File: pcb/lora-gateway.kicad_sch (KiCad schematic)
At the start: 2 parts, among them U1 RFM95W-868S2, U2 ATmega2560-16A

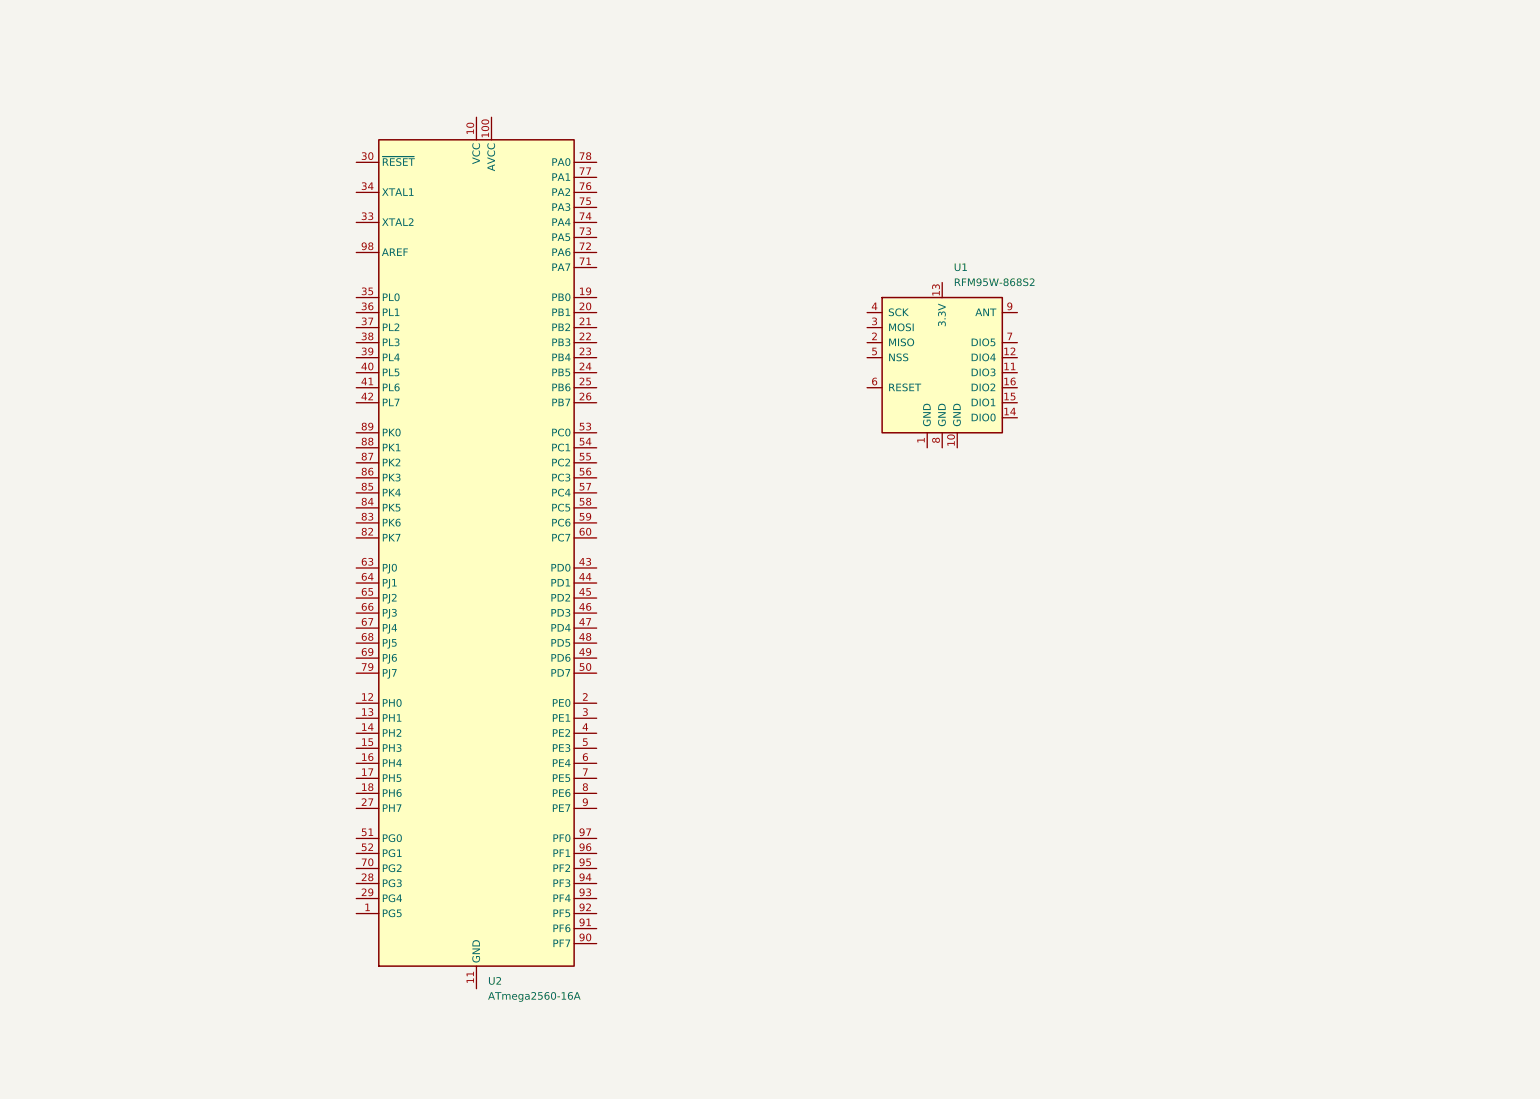
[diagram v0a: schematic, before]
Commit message: add m2560 + rfm95
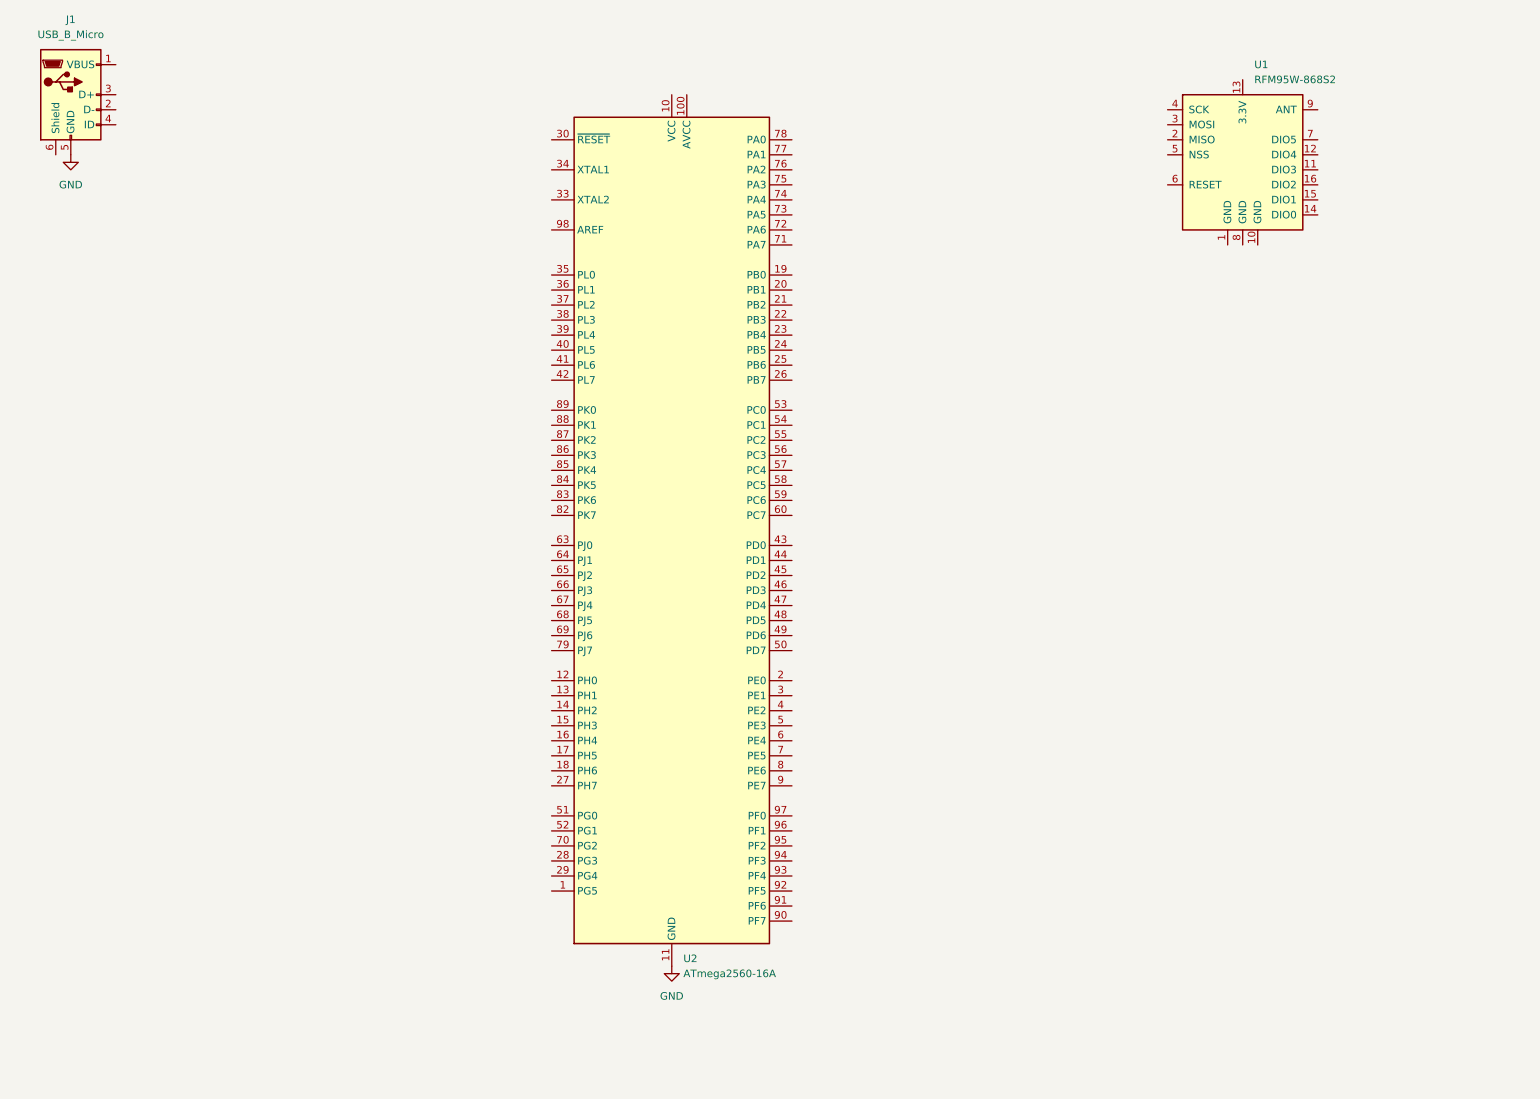
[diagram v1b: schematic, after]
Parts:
- added J1: USB_B_Micro, symbol Connector:USB_B_Micro
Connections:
- net GND: now reaches U2.11 (GND), U2.32 (GND), U2.62 (GND), U2.81 (GND), U2.99 (GND)
- net GND: now also J1.5 (GND)
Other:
- moved on the sheet: U1, U2
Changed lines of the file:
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@@
 (kicad_sch (version 20230121) (generator eeschema)
   (paper "A4")
-  (symbol (lib_id "MCU_Microchip_ATmega:ATmega2560-16A") (at 91.44 102.87 0) (unit 1)
-    (in_bom yes) (on_board yes) (dnp no) (fields_autoplaced)
-    (property "Reference" "U2" (at 93.3959 175.26 0)
-      (effects (font (size 1.27 1.27)) (justify left))
-    )
-    (property "Value" "ATmega2560-16A" (at 93.3959 177.8 0)
-      (effects (font (size 1.27 1.27)) (justify left))
-    )
-    (property "Footprint" "Package_QFP:TQFP-100_14x14mm_P0.5mm" (at 91.44 102.87 0)
+  (symbol (lib_id "MCU_Microchip_ATmega:ATmega2560-16A") (at 124.46 99.06 0) (unit 1)
+    (in_bom yes) (on_board yes) (dnp no) (fields_autoplaced)
+    (property "Reference" "U2" (at 126.4159 171.45 0)
+      (effects (font (size 1.27 1.27)) (justify left))
+    )
+    (property "Value" "ATmega2560-16A" (at 126.4159 173.99 0)
+      (effects (font (size 1.27 1.27)) (justify left))
+    )
+    (property "Footprint" "Package_QFP:TQFP-100_14x14mm_P0.5mm" (at 124.46 99.06 0)
       (effects (font (size 1.27 1.27) italic) hide)
     )
-    (property "Datasheet" "http://ww1.microchip.com/downloads/en/DeviceDoc/Atmel-2549-8-bit-AVR-Microcontroller-ATmega640-1280-1281-2560-2561_datasheet.pdf" (at 91.44 102.87 0)
+    (property "Datasheet" "http://ww1.microchip.com/downloads/en/DeviceDoc/Atmel-2549-8-bit-AVR-Microcontroller-ATmega640-1280-1281-2560-2561_datasheet.pdf" (at 124.46 99.06 0)
       (effects (font (size 1.27 1.27)) hide)
     )
@@
     )
   )
-  (symbol (lib_id "RF_Module:RFM95W-868S2") (at 170.18 69.85 0) (unit 1)
-    (in_bom yes) (on_board yes) (dnp no) (fields_autoplaced)
-    (property "Reference" "U1" (at 172.1359 54.61 0)
-      (effects (font (size 1.27 1.27)) (justify left))
-    )
-    (property "Value" "RFM95W-868S2" (at 172.1359 57.15 0)
-      (effects (font (size 1.27 1.27)) (justify left))
-    )
-    (property "Footprint" "" (at 86.36 27.94 0)
-      (effects (font (size 1.27 1.27)) hide)
-    )
-    (property "Datasheet" "https://www.hoperf.com/data/upload/portal/20181127/5bfcbea20e9ef.pdf" (at 86.36 27.94 0)
+  (symbol (lib_id "Connector:USB_B_Micro") (at 22.86 25.4 0) (unit 1)
+    (in_bom yes) (on_board yes) (dnp no) (fields_autoplaced)
+    (property "Reference" "J1" (at 22.86 12.7 0)
+      (effects (font (size 1.27 1.27)))
+    )
+    (property "Value" "USB_B_Micro" (at 22.86 15.24 0)
+      (effects (font (size 1.27 1.27)))
+    )
+    (property "Footprint" "" (at 26.67 26.67 0)
+      (effects (font (size 1.27 1.27)) hide)
+    )
+    (property "Datasheet" "~" (at 26.67 26.67 0)
+      (effects (font (size 1.27 1.27)) hide)
+    )
+    (pin "1")
+    (pin "2")
+    (pin "3")
+    (pin "4")
+    (pin "5")
+    (pin "6")
+    (instances
+      (project "lora-gateway"
+        (path "/5fd0eb65-7f10-4bbb-b642-b528dcb1ea0e"
+          (reference "J1") (unit 1)
+        )
+      )
+    )
+  )
+  (symbol (lib_id "RF_Module:RFM95W-868S2") (at 220.98 35.56 0) (unit 1)
+    (in_bom yes) (on_board yes) (dnp no) (fields_autoplaced)
+    (property "Reference" "U1" (at 222.9359 20.32 0)
+      (effects (font (size 1.27 1.27)) (justify left))
+    )
+    (property "Value" "RFM95W-868S2" (at 222.9359 22.86 0)
+      (effects (font (size 1.27 1.27)) (justify left))
+    )
+    (property "Footprint" "" (at 137.16 -6.35 0)
+      (effects (font (size 1.27 1.27)) hide)
+    )
+    (property "Datasheet" "https://www.hoperf.com/data/upload/portal/20181127/5bfcbea20e9ef.pdf" (at 137.16 -6.35 0)
       (effects (font (size 1.27 1.27)) hide)
     )
@@
         )
       )
+    )
+  )
+  (symbol (lib_id "power:GND") (at 22.86 35.56 0) (unit 1)
+    (in_bom yes) (on_board yes) (dnp no) (fields_autoplaced)
+    (property "Reference" "#PWR01" (at 22.86 41.91 0)
+      (effects (font (size 1.27 1.27)) hide)
+    )
+    (property "Value" "GND" (at 22.86 40.64 0)
+      (effects (font (size 1.27 1.27)))
+    )
+    (property "Footprint" "" (at 22.86 35.56 0)
+      (effects (font (size 1.27 1.27)) hide)
+    )
+    (property "Datasheet" "" (at 22.86 35.56 0)
+      (effects (font (size 1.27 1.27)) hide)
+    )
+    (pin "1")
+    (instances
+      (project "lora-gateway"
+        (path "/5fd0eb65-7f10-4bbb-b642-b528dcb1ea0e"
+          (reference "#PWR01") (unit 1)
+        )
+      )
+    )
+  )
+  (symbol (lib_id "power:GND") (at 124.46 172.72 0) (unit 1)
+    (in_bom yes) (on_board yes) (dnp no) (fields_autoplaced)
+    (property "Reference" "#PWR02" (at 124.46 179.07 0)
+      (effects (font (size 1.27 1.27)) hide)
+    )
+    (property "Value" "GND" (at 124.46 177.8 0)
+      (effects (font (size 1.27 1.27)))
+    )
+    (property "Footprint" "" (at 124.46 172.72 0)
+      (effects (font (size 1.27 1.27)) hide)
+    )
+    (property "Datasheet" "" (at 124.46 172.72 0)
+      (effects (font (size 1.27 1.27)) hide)
+    )
+    (pin "1")
+    (instances
+      (project "lora-gateway"
+        (path "/5fd0eb65-7f10-4bbb-b642-b528dcb1ea0e"
+          (reference "#PWR02") (unit 1)
+        )
+      )

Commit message: add board + usr es1 connector
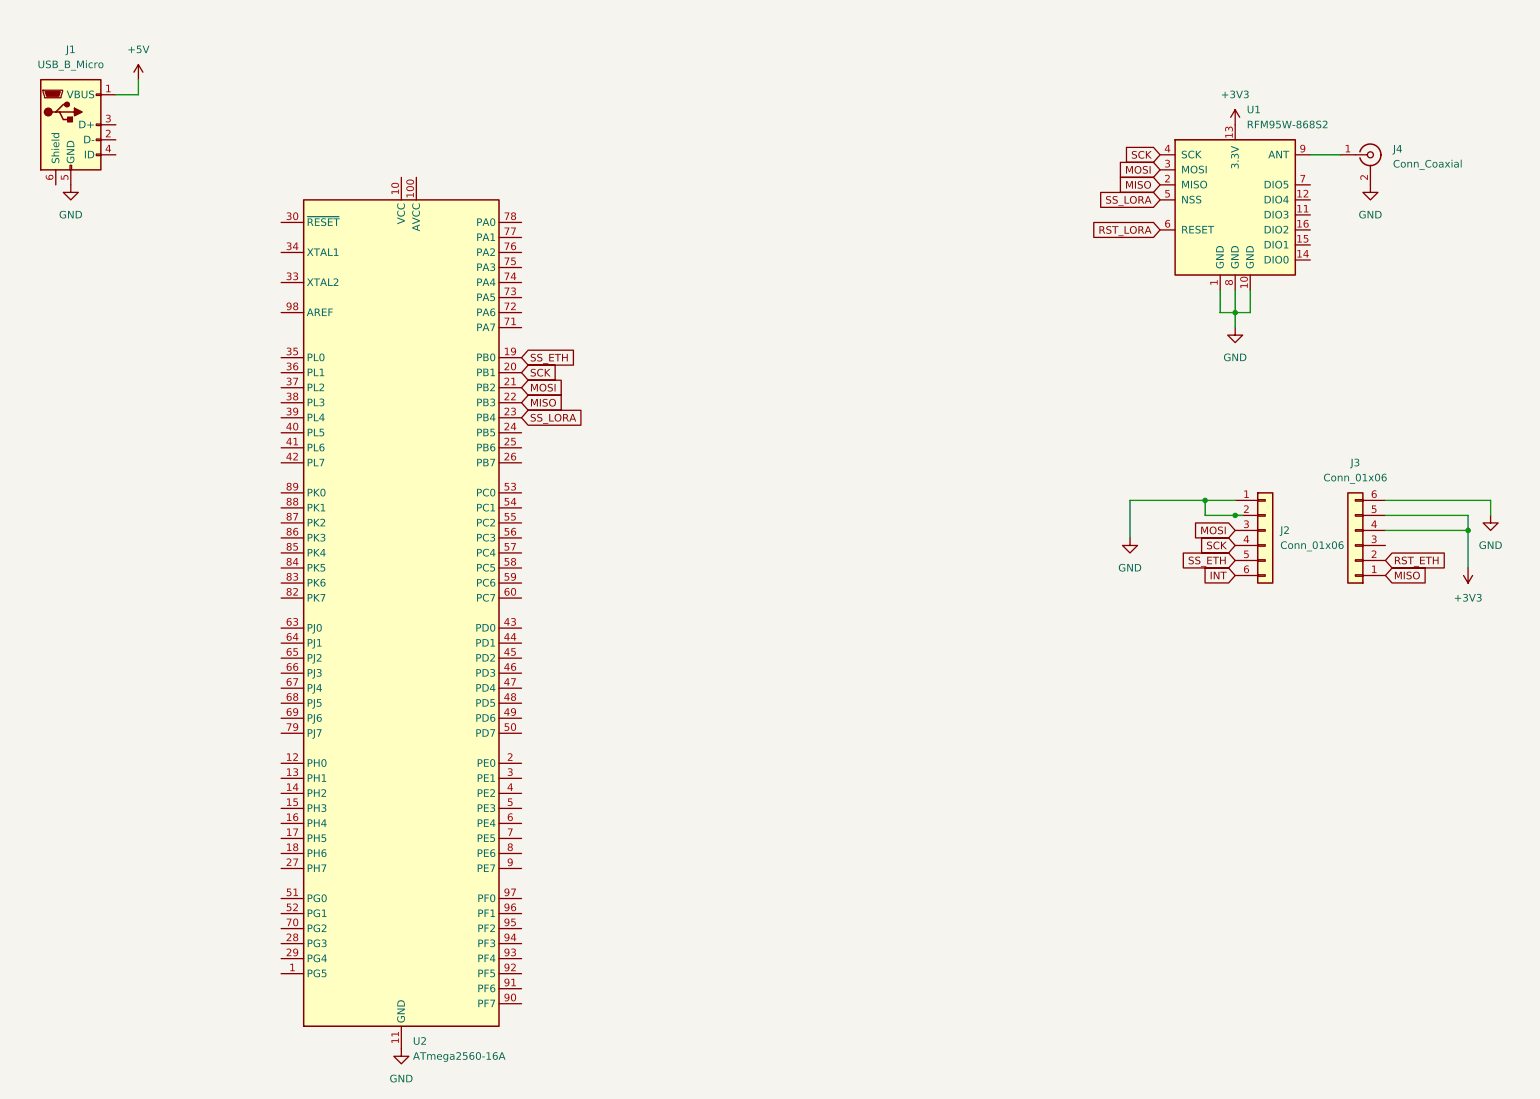
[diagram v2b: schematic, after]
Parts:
- added J2, J3: Conn_01x06, Connector_PinHeader_2.54mm:PinHeader_1x06_P2.54mm_Vertical, symbol Connector_Generic:Conn_01x06
- added J4: Conn_Coaxial, Connector_Coaxial:SMA_Molex_73251-2120_EdgeMount_Horizontal, symbol Connector:Conn_Coaxial
- J1: footprint (none) -> Connector_USB:USB_Micro-B_Amphenol_10103594-0001LF_Horizontal
- U1: footprint (none) -> RF_Module:HOPERF_RFM9XW_SMD
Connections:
- net GND: now also U1.1 (GND), U1.10 (GND), U1.8 (GND), J2.1 (Pin_1), J2.2 (Pin_2), J3.6 (Pin_6), J4.2 (Ext)
- net SS_ETH: now reaches U2.19 (PB0)
- net SS_ETH: now also J2.5 (Pin_5)
- net SCK: now reaches U2.20 (PB1)
- net SCK: now also U1.4 (SCK), J2.4 (Pin_4)
- net MOSI: now reaches U2.21 (PB2)
- net MOSI: now also U1.3 (MOSI), J2.3 (Pin_3)
- net MISO: now reaches U2.22 (PB3)
- net MISO: now also U1.2 (MISO), J3.1 (Pin_1)
- net SS_LORA: now reaches U2.23 (PB4)
- net SS_LORA: now also U1.5 (NSS)
- net +5V: now reaches J1.1 (VBUS)
- net +3V3: now reaches U1.13 (3.3V)
- net +3V3: now also J3.4 (Pin_4), J3.5 (Pin_5)
- net RST_LORA: now reaches U1.6 (RESET)
- net at U1.9 (ANT): now also J4.1 (In)
- new net INT: J2.6 (Pin_6)
- new net RST_ETH: J3.2 (Pin_2)
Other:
- moved on the sheet: J1, U1, U2
